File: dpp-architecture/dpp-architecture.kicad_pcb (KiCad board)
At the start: 2 copper layers, 111.8 x 76.2 mm, 21 parts, among them J1 OSTYK51102030, J2 OSTYK51102030, J3 Conn_01x03_Male, J4 OSTYK51102030, Q1 IRFU120NPBF, T1 750311659, U1 DGD0215WT-7

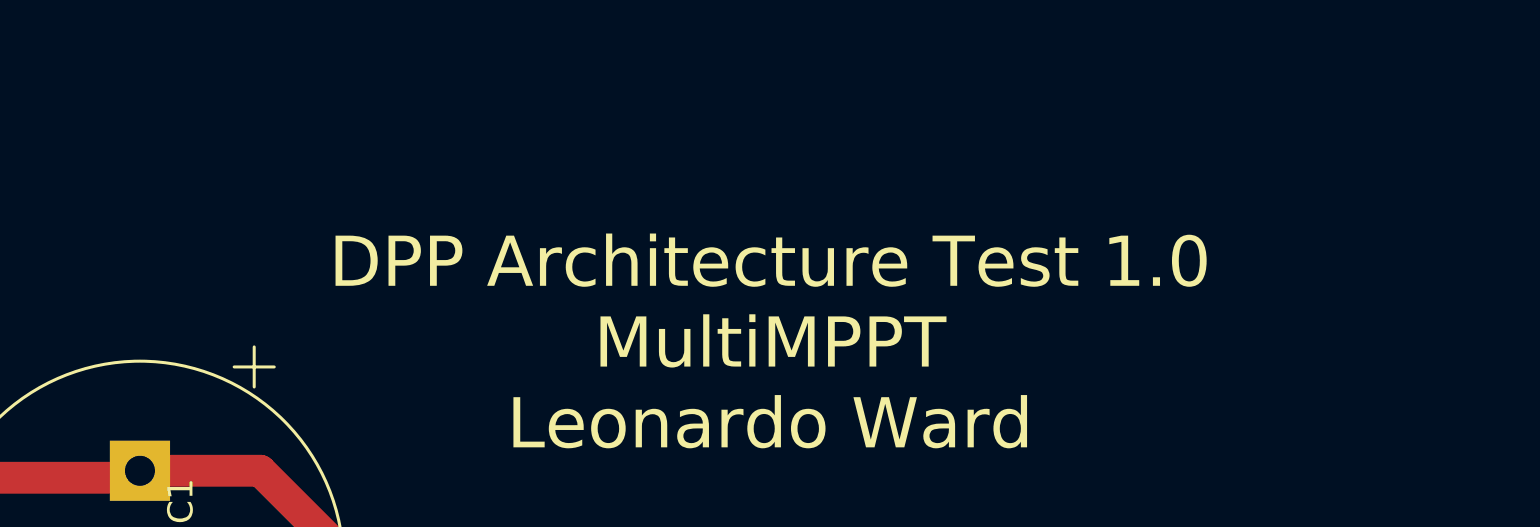
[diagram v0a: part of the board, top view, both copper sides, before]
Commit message: Added documentation to the readme: images of the schematic, pcb and added bill of materials
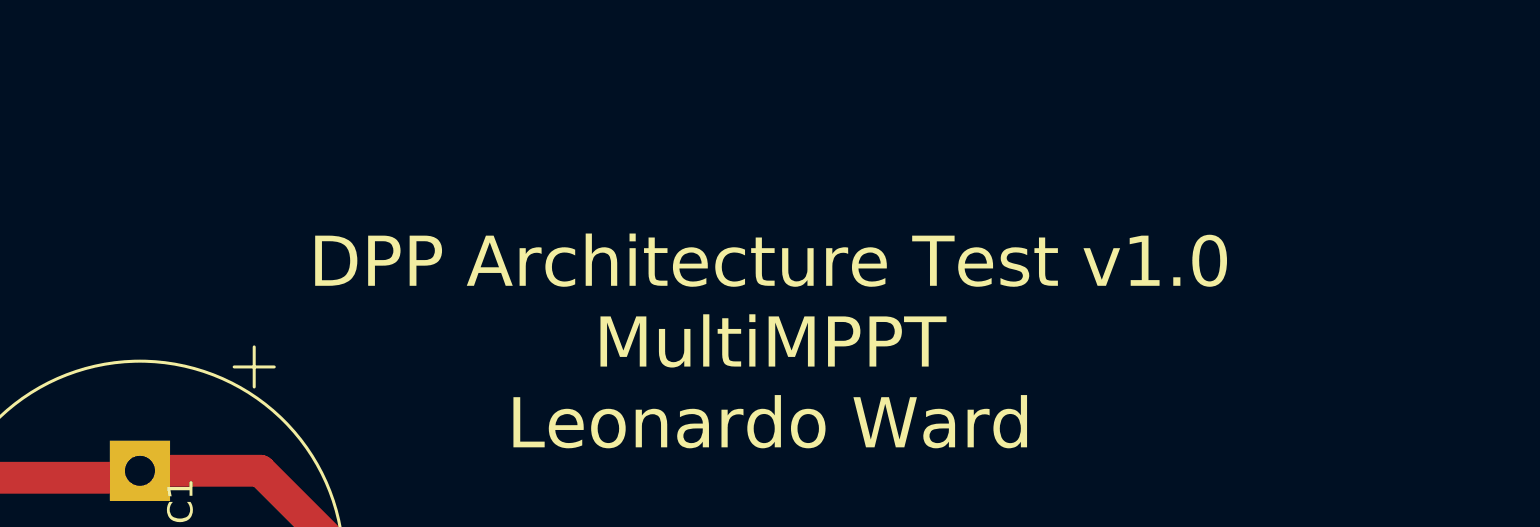
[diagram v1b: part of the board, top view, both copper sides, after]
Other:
- board text added: "DPP Architecture Test v1.0 MultiMPPT Leonardo Ward"
- board text removed: "DPP Architecture Test 1.0 MultiMPPT Leonardo Ward"
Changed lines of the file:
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@@
     (effects (font (size 1 1) (thickness 0.15)))
   )
-  (gr_text "DPP Architecture Test 1.0\nMultiMPPT\nLeonardo Ward" (at 160.02 73.66) (layer "F.SilkS")
+  (gr_text "DPP Architecture Test v1.0\nMultiMPPT\nLeonardo Ward" (at 160.02 73.66) (layer "F.SilkS")
     (effects (font (size 2 2) (thickness 0.3)))
   )
